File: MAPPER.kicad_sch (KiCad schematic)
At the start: 18 parts

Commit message: added more notes and documentation
todo:
    - timing analysis to make sure everything fits in 250nS + hold time/prep time
    - logic analysis to ensure correct functionality (am gonna make dumb mistakes!)
    - board layout
    - physical testing!
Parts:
- removed U? (x4): 74LS573, symbol 74xx:74LS573
- added U?: (no value), symbol 74xx:74AHC273
- added U? (x3): 74AHC273, symbol 74xx:74AHC273
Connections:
- net +5V: now also U?.20 (VCC), U?.20 (VCC), U?.20 (VCC), U?.20 (VCC)
- net DB_{0}: now also U?.3 (D0), U?.3 (D0), U?.3 (D0), U?.3 (D0)
- net DB_{1}: now also U?.4 (D1), U?.4 (D1), U?.4 (D1), U?.4 (D1)
- net DB_{2}: now also U?.7 (D2), U?.7 (D2), U?.7 (D2), U?.7 (D2)
- net DB_{3}: now also U?.8 (D3), U?.8 (D3), U?.8 (D3), U?.8 (D3)
- net DB_{4}: now also U?.13 (D4), U?.13 (D4), U?.13 (D4), U?.13 (D4)
- net DB_{5}: now also U?.14 (D5), U?.14 (D5), U?.14 (D5), U?.14 (D5)
- net DB_{6}: now also U?.17 (D6), U?.17 (D6), U?.17 (D6), U?.17 (D6)
- net DB_{7}: now also U?.18 (D7), U?.18 (D7), U?.18 (D7), U?.18 (D7)
- net GND: now also U?.10 (GND), U?.10 (GND), U?.10 (GND), U?.10 (GND)
- net PAN_{1}_{0}: now also U?.2 (Q0)
- net PAN_{1}_{1}: now also U?.5 (Q1)
- net PAN_{1}_{2}: now also U?.6 (Q2)
- net PAN_{1}_{3}: now also U?.9 (Q3)
- net PAN_{1}_{4}: now also U?.12 (Q4)
- net PAN_{1}_{5}: now also U?.15 (Q5)
- net PAN_{1}_{6}: now also U?.16 (Q6)
- net PAN_{1}_{7}: now also U?.19 (Q7)
- net PAN_{2}_{0}: now also U?.2 (Q0)
- net PAN_{2}_{1}: now also U?.5 (Q1)
- net PAN_{2}_{2}: now also U?.6 (Q2)
- net PAN_{2}_{3}: now also U?.9 (Q3)
- net PAN_{2}_{4}: now also U?.12 (Q4)
- net PAN_{2}_{5}: now also U?.15 (Q5)
- net PAN_{2}_{6}: now also U?.16 (Q6)
- net PAN_{2}_{7}: now also U?.19 (Q7)
- net PAN_{3}_{0}: now also U?.2 (Q0)
- net PAN_{3}_{1}: now also U?.5 (Q1)
- net PAN_{3}_{2}: now also U?.6 (Q2)
- net PAN_{3}_{3}: now also U?.9 (Q3)
- net PAN_{3}_{4}: now also U?.12 (Q4)
- net PAN_{3}_{5}: now also U?.15 (Q5)
- net PAN_{3}_{6}: now also U?.16 (Q6)
- net PAN_{3}_{7}: now also U?.19 (Q7)
- net PAN_{4}_{0}: now also U?.2 (Q0)
- net PAN_{4}_{1}: now also U?.5 (Q1)
- net PAN_{4}_{2}: now also U?.6 (Q2)
- net PAN_{4}_{3}: now also U?.9 (Q3)
- net PAN_{4}_{4}: now also U?.12 (Q4)
- net PAN_{4}_{5}: now also U?.15 (Q5)
- net PAN_{4}_{6}: now also U?.16 (Q6)
- net PAN_{4}_{7}: now also U?.19 (Q7)
- net ~{RST}: now also U?.1 (~{Mr}), U?.1 (~{Mr}), U?.1 (~{Mr}), U?.1 (~{Mr})
- net at U?.4: now also U?.11 (Cp) (x4)

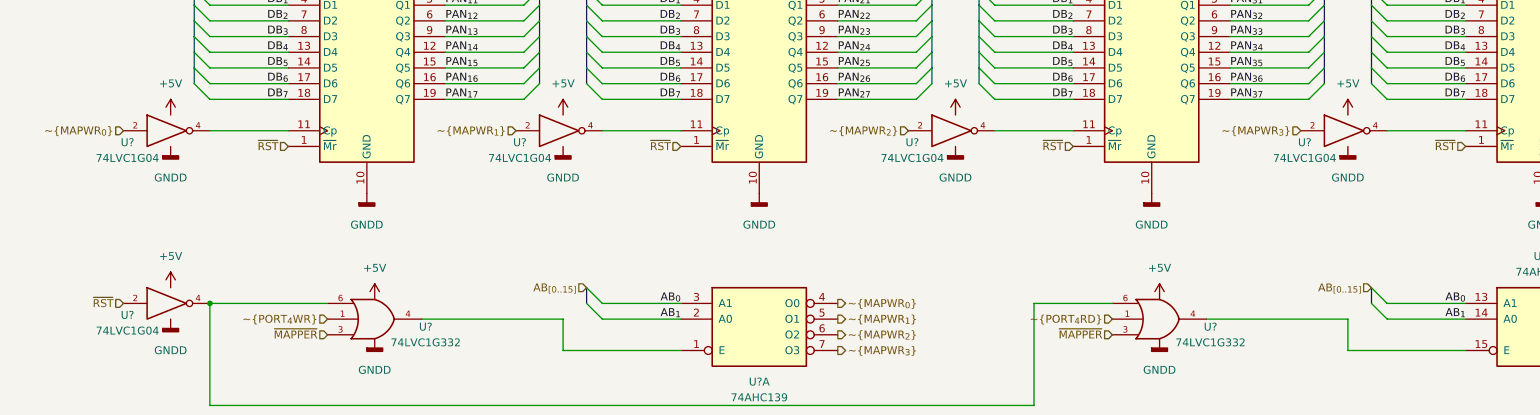
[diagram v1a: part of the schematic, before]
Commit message: fixed non obvious bug in mapper circuit reset logic, would be possible to have the latches both clocked and reset at the same time!, now only resets when in reset, and only clocks when not in reset
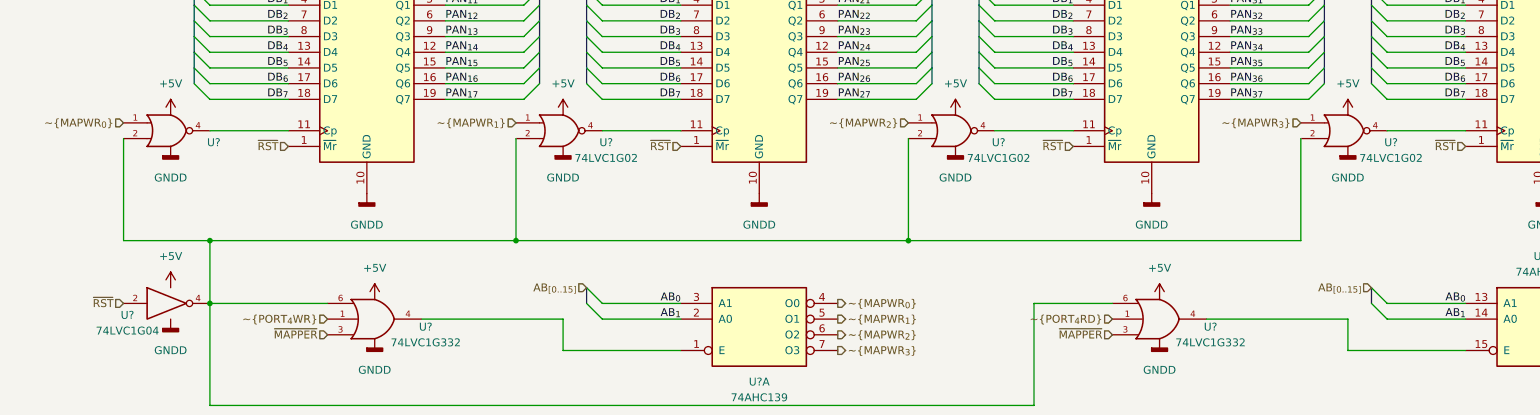
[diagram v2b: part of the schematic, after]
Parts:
- removed U? (x4): 74LVC1G04, symbol 74xGxx:74LVC1G04
- added U? (x3): 74LVC1G02, symbol 74xGxx:74LVC1G02
- added U?: (no value), symbol 74xGxx:74LVC1G02
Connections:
- net +5V: now also U?.5 (VCC), U?.5 (VCC), U?.5 (VCC), U?.5 (VCC)
- net GND: now also U?.3 (GND), U?.3 (GND), U?.3 (GND), U?.3 (GND)
- net ~{MAPWR_{0}}: now also U?.1
- net ~{MAPWR_{1}}: now also U?.1
- net ~{MAPWR_{2}}: now also U?.1
- net ~{MAPWR_{3}}: now also U?.1
- net at U?.11 (Cp): now also U?.4 (x4)
- net at U?.4, U?.6, U?.6: now also U?.2, U?.2, U?.2, U?.2

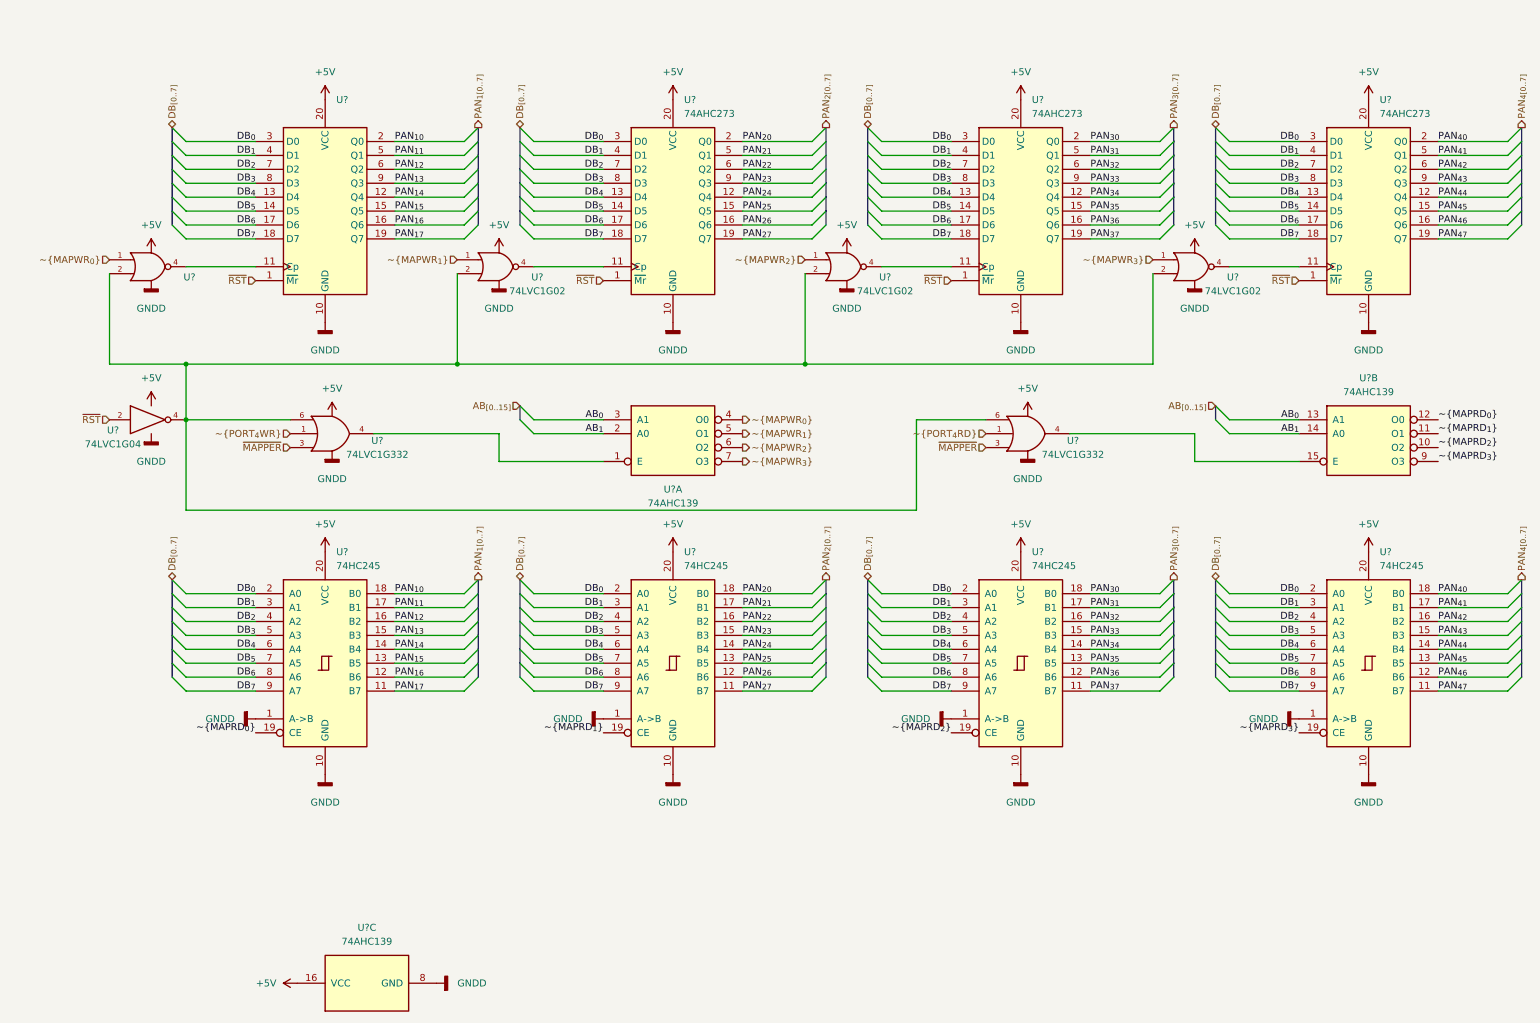
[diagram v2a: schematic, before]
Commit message: changed bus names to avoid possible conflicts, fixed unnamed busses.
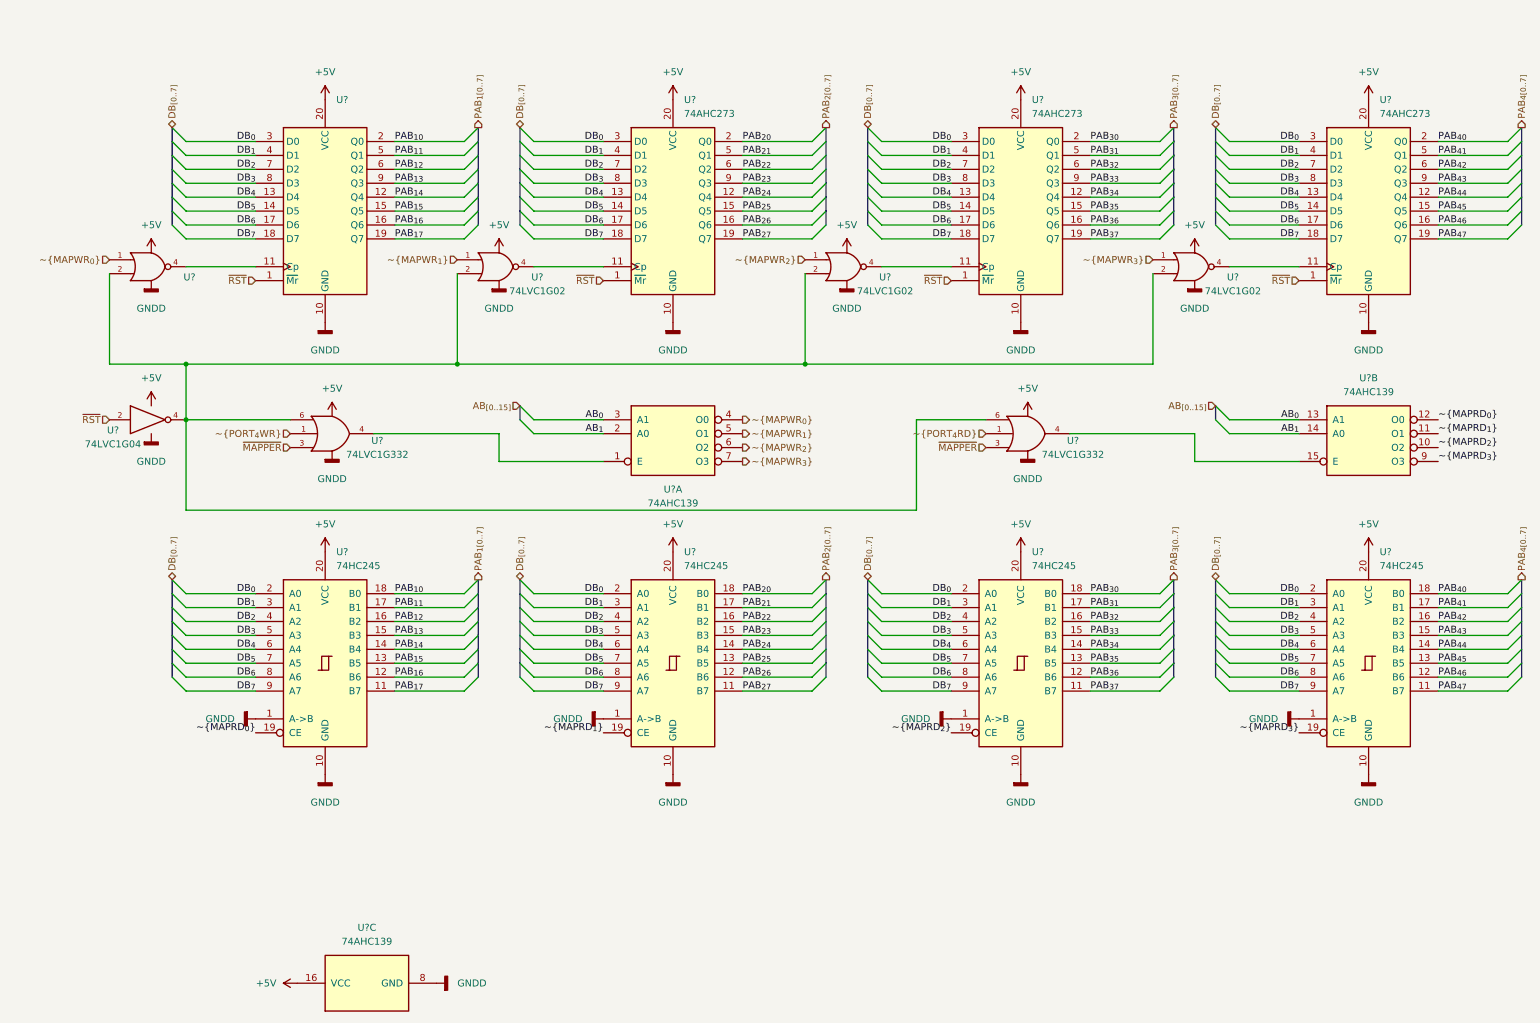
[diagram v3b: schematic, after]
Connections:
- net PAN_{1}_{0} renamed PAB_{1}_{0}
- net PAN_{1}_{1} renamed PAB_{1}_{1}
- net PAN_{1}_{2} renamed PAB_{1}_{2}
- net PAN_{1}_{3} renamed PAB_{1}_{3}
- net PAN_{1}_{4} renamed PAB_{1}_{4}
- net PAN_{1}_{5} renamed PAB_{1}_{5}
- net PAN_{1}_{6} renamed PAB_{1}_{6}
- net PAN_{1}_{7} renamed PAB_{1}_{7}
- net PAN_{2}_{0} renamed PAB_{2}_{0}
- net PAN_{2}_{1} renamed PAB_{2}_{1}
- net PAN_{2}_{2} renamed PAB_{2}_{2}
- net PAN_{2}_{3} renamed PAB_{2}_{3}
- net PAN_{2}_{4} renamed PAB_{2}_{4}
- net PAN_{2}_{5} renamed PAB_{2}_{5}
- net PAN_{2}_{6} renamed PAB_{2}_{6}
- net PAN_{2}_{7} renamed PAB_{2}_{7}
- net PAN_{3}_{0} renamed PAB_{3}_{0}
- net PAN_{3}_{1} renamed PAB_{3}_{1}
- net PAN_{3}_{2} renamed PAB_{3}_{2}
- net PAN_{3}_{3} renamed PAB_{3}_{3}
- net PAN_{3}_{4} renamed PAB_{3}_{4}
- net PAN_{3}_{5} renamed PAB_{3}_{5}
- net PAN_{3}_{6} renamed PAB_{3}_{6}
- net PAN_{3}_{7} renamed PAB_{3}_{7}
- net PAN_{4}_{0} renamed PAB_{4}_{0}
- net PAN_{4}_{1} renamed PAB_{4}_{1}
- net PAN_{4}_{2} renamed PAB_{4}_{2}
- net PAN_{4}_{3} renamed PAB_{4}_{3}
- net PAN_{4}_{4} renamed PAB_{4}_{4}
- net PAN_{4}_{5} renamed PAB_{4}_{5}
- net PAN_{4}_{6} renamed PAB_{4}_{6}
- net PAN_{4}_{7} renamed PAB_{4}_{7}

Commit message: added decoupling capacitors, perhaps too many? idk better more than less!
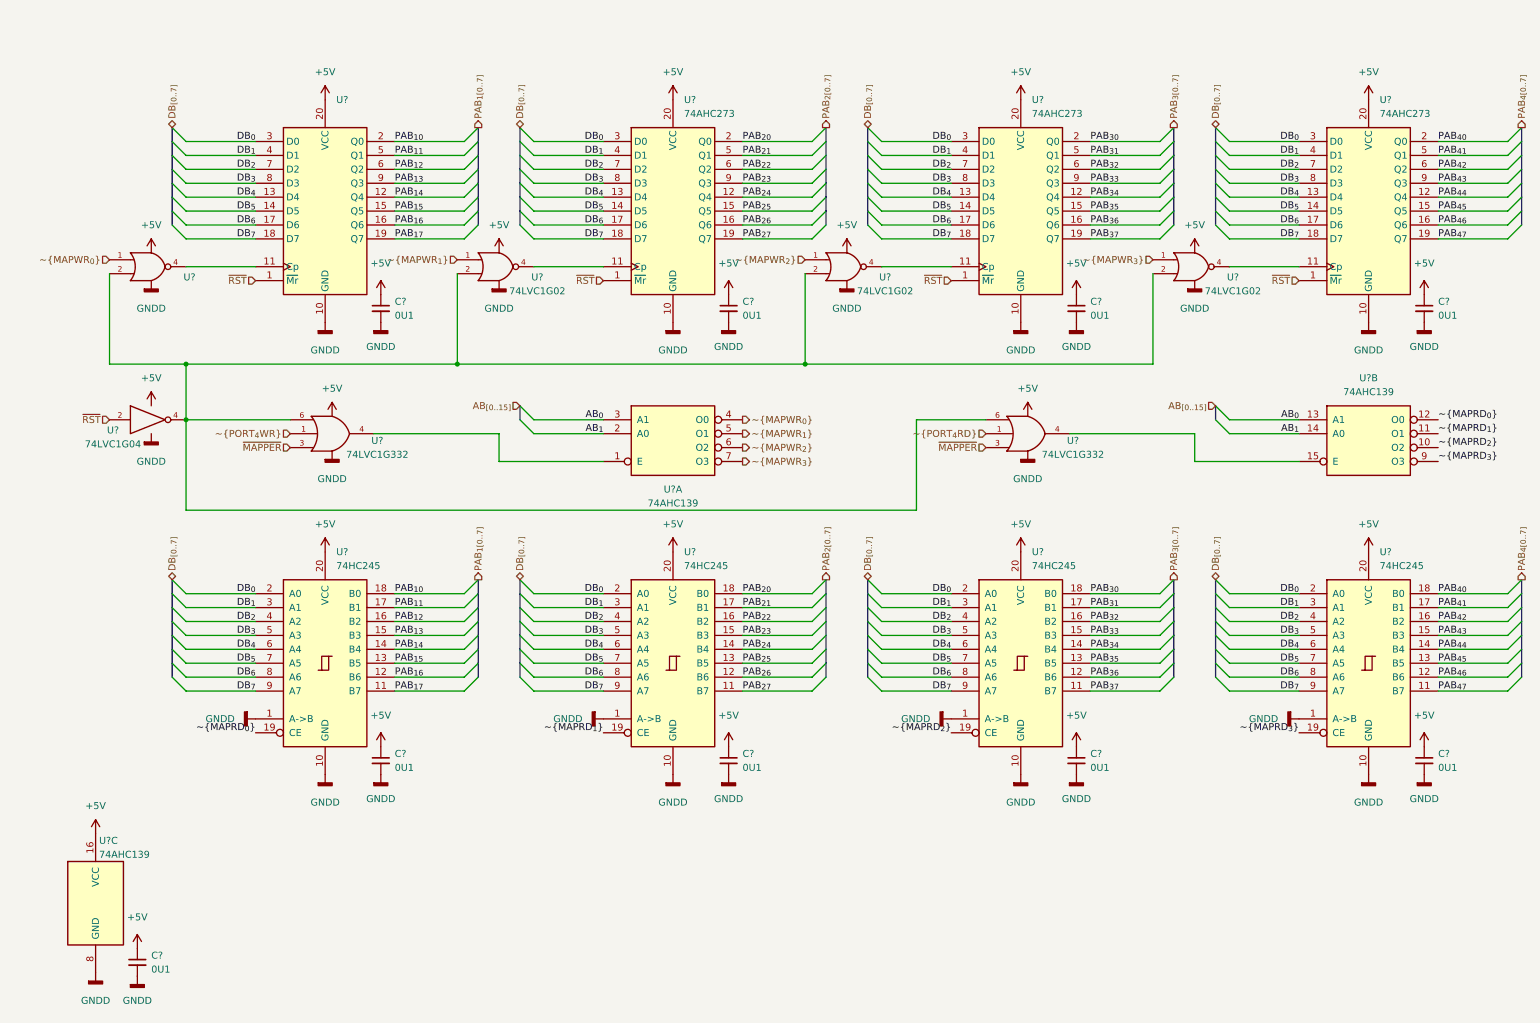
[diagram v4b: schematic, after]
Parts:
- added C? (x9): 0U1, symbol Device:C_Small
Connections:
- net +5V: now also C?.1, C?.1, C?.1, C?.1, C?.1, C?.1, C?.1, C?.1, C?.1
- net GND: now also C?.2, C?.2, C?.2, C?.2, C?.2, C?.2, C?.2, C?.2, C?.2
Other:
- moved on the sheet: U?C
